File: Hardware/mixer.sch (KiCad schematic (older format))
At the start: 14 parts, among them U5 TL072

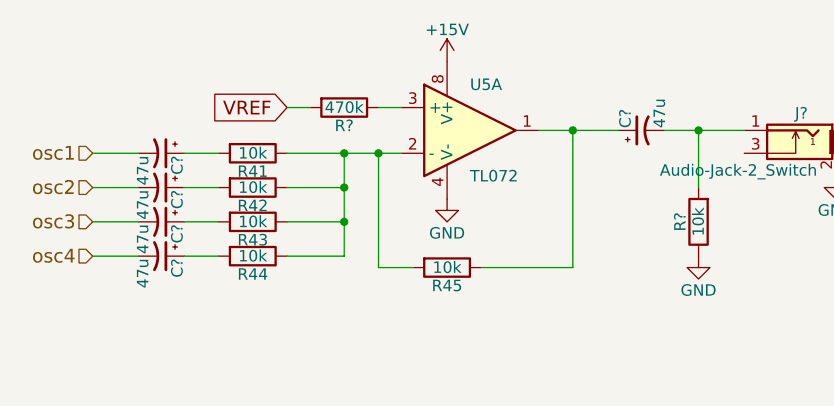
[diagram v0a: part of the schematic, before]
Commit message: change corner frequency of DC blocking caps  everywhere they are in use.  Updated some simulation files to test filter circuits.
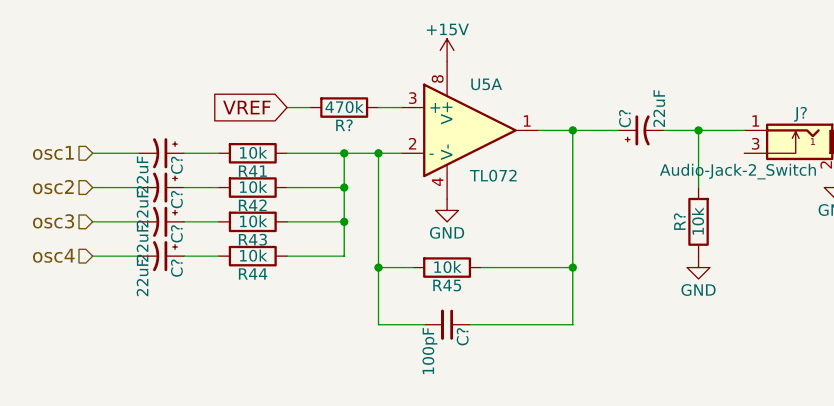
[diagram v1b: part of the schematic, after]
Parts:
- added C?: 100pF, symbol C_Small
- C? (x5): value 47u -> 22uF
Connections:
- net at R41.1, R42.1, R43.1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: now also C?.2
- net at C?.1, R45.1, U5.1: now also C?.1
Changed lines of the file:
@@
 	6200 4100 6600 4100
 Wire Wire Line
-	6600 4100 6600 3500
+	6600 3500 6600 4350
 Wire Wire Line
 	5900 4100 5750 4100
 Wire Wire Line
-	5750 3600 5750 4100
+	5750 3600 5750 4350
 Wire Wire Line
 	5350 3600 5850 3600
@@
 P 4800 3600
 F 0 "C?" H 4810 3670 50  0000 L CNN
-F 1 "47u" H 4810 3520 50  0000 L CNN
+F 1 "22uF" H 4810 3520 50  0000 L CNN
 F 2 "" H 4800 3600 50  0001 C CNN
 F 3 "" H 4800 3600 50  0001 C CNN
@@
 P 4800 3750
 F 0 "C?" H 4810 3820 50  0000 L CNN
-F 1 "47u" H 4810 3670 50  0000 L CNN
+F 1 "22uF" H 4810 3670 50  0000 L CNN
 F 2 "" H 4800 3750 50  0001 C CNN
 F 3 "" H 4800 3750 50  0001 C CNN
@@
 P 4800 3900
 F 0 "C?" H 4810 3970 50  0000 L CNN
-F 1 "47u" H 4810 3820 50  0000 L CNN
+F 1 "22uF" H 4810 3820 50  0000 L CNN
 F 2 "" H 4800 3900 50  0001 C CNN
 F 3 "" H 4800 3900 50  0001 C CNN
@@
 P 4800 4050
 F 0 "C?" H 4810 4120 50  0000 L CNN
-F 1 "47u" H 4810 3970 50  0000 L CNN
+F 1 "22uF" H 4810 3970 50  0000 L CNN
 F 2 "" H 4800 4050 50  0001 C CNN
 F 3 "" H 4800 4050 50  0001 C CNN
@@
 P 6900 3500
 F 0 "C?" H 6910 3570 50  0000 L CNN
-F 1 "47u" H 6910 3420 50  0000 L CNN
+F 1 "22uF" H 6910 3420 50  0000 L CNN
 F 2 "" H 6900 3500 50  0001 C CNN
 F 3 "" H 6900 3500 50  0001 C CNN
@@
 Wire Wire Line
 	5350 3400 5450 3400
+$Comp
+L C_Small C?
+U 1 1 5C37DB67
+P 6050 4350
+F 0 "C?" H 6060 4420 50  0000 L CNN
+F 1 "100pF" H 6060 4270 50  0000 L CNN
+F 2 "" H 6050 4350 50  0001 C CNN
+F 3 "" H 6050 4350 50  0001 C CNN
+	1    6050 4350
+	0    1    1    0
+$EndComp
+Wire Wire Line
+	6600 4350 6150 4350
+Connection ~ 6600 4100
+Wire Wire Line
+	5750 4350 5950 4350
+Connection ~ 5750 4100
 $EndSCHEMATC

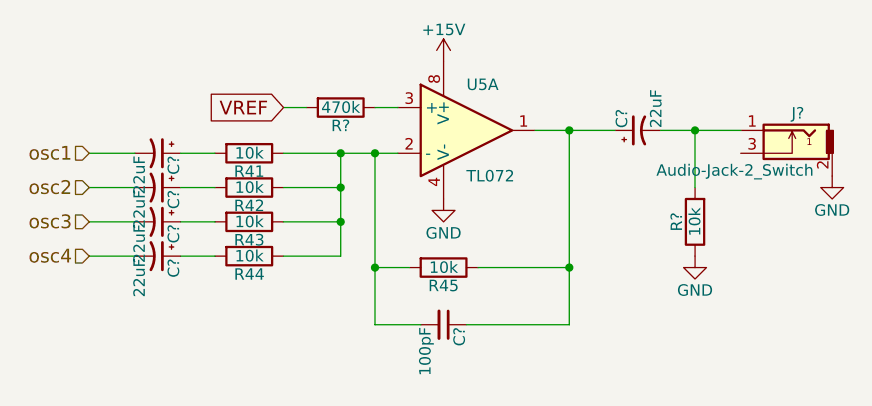
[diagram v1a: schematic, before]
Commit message: associate footprints with all components
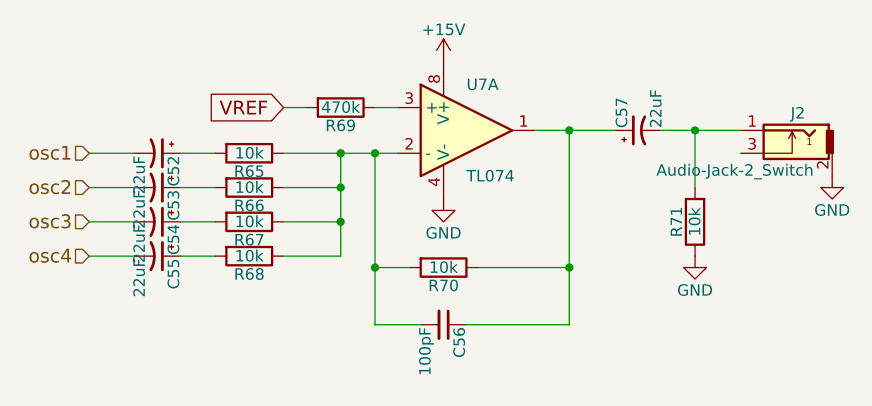
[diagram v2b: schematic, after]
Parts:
- C52, C53, C54, C55, C57: renamed from C?; footprint (none) -> Capacitors_SMD:CP_Elec_5x5.7
- C56: renamed from C?; footprint (none) -> digikey-footprints:0805
- J2: renamed from J?; footprint (none) -> Connectors:PINHEAD1-3
- R65: renamed from R41; footprint (none) -> digikey-footprints:0805
- R66: renamed from R42; footprint (none) -> digikey-footprints:0805
- R67: renamed from R43; footprint (none) -> digikey-footprints:0805
- R68: renamed from R44; footprint (none) -> digikey-footprints:0805
- R69, R71: renamed from R?; footprint (none) -> digikey-footprints:0805
- R70: renamed from R45; footprint (none) -> digikey-footprints:0805
- U7: renamed from U5; value TL072 -> TL074; footprint (none) -> digikey-footprints:Humidity_SHT15
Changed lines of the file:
@@
 osc4
 $Comp
-L R R41
+L R R65
 U 1 1 5C368A69
 P 5200 3600
-F 0 "R41" V 5280 3600 50  0000 C CNN
+F 0 "R65" V 5280 3600 50  0000 C CNN
 F 1 "10k" V 5200 3600 50  0000 C CNN
-F 2 "" V 5130 3600 50  0001 C CNN
+F 2 "digikey-footprints:0805" V 5130 3600 50  0001 C CNN
 F 3 "" H 5200 3600 50  0001 C CNN
 	1    5200 3600
@@
 $EndComp
 $Comp
-L R R42
+L R R66
 U 1 1 5C368B13
 P 5200 3750
-F 0 "R42" V 5280 3750 50  0000 C CNN
+F 0 "R66" V 5280 3750 50  0000 C CNN
 F 1 "10k" V 5200 3750 50  0000 C CNN
-F 2 "" V 5130 3750 50  0001 C CNN
+F 2 "digikey-footprints:0805" V 5130 3750 50  0001 C CNN
 F 3 "" H 5200 3750 50  0001 C CNN
 	1    5200 3750
@@
 $EndComp
 $Comp
-L R R43
+L R R67
 U 1 1 5C368B2B
 P 5200 3900
-F 0 "R43" V 5280 3900 50  0000 C CNN
+F 0 "R67" V 5280 3900 50  0000 C CNN
 F 1 "10k" V 5200 3900 50  0000 C CNN
-F 2 "" V 5130 3900 50  0001 C CNN
+F 2 "digikey-footprints:0805" V 5130 3900 50  0001 C CNN
 F 3 "" H 5200 3900 50  0001 C CNN
 	1    5200 3900
@@
 $EndComp
 $Comp
-L R R44
+L R R68
 U 1 1 5C368B46
 P 5200 4050
-F 0 "R44" V 5280 4050 50  0000 C CNN
+F 0 "R68" V 5280 4050 50  0000 C CNN
 F 1 "10k" V 5200 4050 50  0000 C CNN
-F 2 "" V 5130 4050 50  0001 C CNN
+F 2 "digikey-footprints:0805" V 5130 4050 50  0001 C CNN
 F 3 "" H 5200 4050 50  0001 C CNN
 	1    5200 4050
@@
 	4500 4050 4700 4050
 $Comp
-L TL072 U5
+L TL072 U7
 U 1 1 5C368C88
 P 6150 3500
-F 0 "U5" H 6150 3700 50  0000 L CNN
-F 1 "TL072" H 6150 3300 50  0000 L CNN
-F 2 "" H 6150 3500 50  0001 C CNN
+F 0 "U7" H 6150 3700 50  0000 L CNN
+F 1 "TL074" H 6150 3300 50  0000 L CNN
+F 2 "digikey-footprints:Humidity_SHT15" H 6150 3500 50  0001 C CNN
 F 3 "" H 6150 3500 50  0001 C CNN
 	1    6150 3500
@@
 $EndComp
 $Comp
-L R R45
+L R R70
 U 1 1 5C368D28
 P 6050 4100
-F 0 "R45" V 6130 4100 50  0000 C CNN
+F 0 "R70" V 6130 4100 50  0000 C CNN
 F 1 "10k" V 6050 4100 50  0000 C CNN
-F 2 "" V 5980 4100 50  0001 C CNN
+F 2 "digikey-footprints:0805" V 5980 4100 50  0001 C CNN
 F 3 "" H 6050 4100 50  0001 C CNN
 	1    6050 4100
@@
 Connection ~ 6600 3500
 $Comp
-L Audio-Jack-2_Switch J?
+L Audio-Jack-2_Switch J2
 U 1 1 5C394BFE
 P 7550 3600
-F 0 "J?" H 7500 3775 50  0000 C CNN
+F 0 "J2" H 7500 3775 50  0000 C CNN
 F 1 "Audio-Jack-2_Switch" H 7775 3525 50  0000 C CNN
-F 2 "" H 7800 3700 50  0001 C CNN
+F 2 "Connectors:PINHEAD1-3" H 7800 3700 50  0001 C CNN
 F 3 "" H 7800 3700 50  0001 C CNN
 	1    7550 3600
@@
 $EndComp
 $Comp
-L GND #PWR?
+L GND #PWR067
 U 1 1 5C394C8E
 P 7750 3700
-F 0 "#PWR?" H 7750 3450 50  0001 C CNN
+F 0 "#PWR067" H 7750 3450 50  0001 C CNN
 F 1 "GND" H 7750 3550 50  0000 C CNN
 F 2 "" H 7750 3700 50  0001 C CNN
@@
 $EndComp
 $Comp
-L CP1_Small C?
+L CP1_Small C52
 U 1 1 5C396119
 P 4800 3600
-F 0 "C?" H 4810 3670 50  0000 L CNN
+F 0 "C52" H 4810 3670 50  0000 L CNN
 F 1 "22uF" H 4810 3520 50  0000 L CNN
-F 2 "" H 4800 3600 50  0001 C CNN
+F 2 "Capacitors_SMD:CP_Elec_5x5.7" H 4800 3600 50  0001 C CNN
 F 3 "" H 4800 3600 50  0001 C CNN
 	1    4800 3600
@@
 $EndComp
 $Comp
-L CP1_Small C?
+L CP1_Small C53
 U 1 1 5C396261
 P 4800 3750
-F 0 "C?" H 4810 3820 50  0000 L CNN
+F 0 "C53" H 4810 3820 50  0000 L CNN
 F 1 "22uF" H 4810 3670 50  0000 L CNN
-F 2 "" H 4800 3750 50  0001 C CNN
+F 2 "Capacitors_SMD:CP_Elec_5x5.7" H 4800 3750 50  0001 C CNN
 F 3 "" H 4800 3750 50  0001 C CNN
 	1    4800 3750
@@
 $EndComp
 $Comp
-L CP1_Small C?
+L CP1_Small C54
 U 1 1 5C39628E
 P 4800 3900
-F 0 "C?" H 4810 3970 50  0000 L CNN
+F 0 "C54" H 4810 3970 50  0000 L CNN
 F 1 "22uF" H 4810 3820 50  0000 L CNN
-F 2 "" H 4800 3900 50  0001 C CNN
+F 2 "Capacitors_SMD:CP_Elec_5x5.7" H 4800 3900 50  0001 C CNN
 F 3 "" H 4800 3900 50  0001 C CNN
 	1    4800 3900
@@
 $EndComp
 $Comp
-L CP1_Small C?
+L CP1_Small C55
 U 1 1 5C3962BE
 P 4800 4050
-F 0 "C?" H 4810 4120 50  0000 L CNN
+F 0 "C55" H 4810 4120 50  0000 L CNN
 F 1 "22uF" H 4810 3970 50  0000 L CNN
-F 2 "" H 4800 4050 50  0001 C CNN
+F 2 "Capacitors_SMD:CP_Elec_5x5.7" H 4800 4050 50  0001 C CNN
 F 3 "" H 4800 4050 50  0001 C CNN
 	1    4800 4050
@@
 	4900 3600 5050 3600
 $Comp
-L GND #PWR?
+L GND #PWR068
 U 1 1 5C396479
 P 6050 3800
-F 0 "#PWR?" H 6050 3550 50  0001 C CNN
+F 0 "#PWR068" H 6050 3550 50  0001 C CNN
 F 1 "GND" H 6050 3650 50  0000 C CNN
 F 2 "" H 6050 3800 50  0001 C CNN
@@
 $EndComp
 $Comp
-L CP1_Small C?
+L CP1_Small C57
 U 1 1 5C3964A5
 P 6900 3500
-F 0 "C?" H 6910 3570 50  0000 L CNN
+F 0 "C57" H 6910 3570 50  0000 L CNN
 F 1 "22uF" H 6910 3420 50  0000 L CNN
-F 2 "" H 6900 3500 50  0001 C CNN
+F 2 "Capacitors_SMD:CP_Elec_5x5.7" H 6900 3500 50  0001 C CNN
 F 3 "" H 6900 3500 50  0001 C CNN
 	1    6900 3500
@@
 	7000 3500 7350 3500
 $Comp
-L R R?
+L R R71
 U 1 1 5C3965C9
 P 7150 3900
-F 0 "R?" V 7230 3900 50  0000 C CNN
+F 0 "R71" V 7230 3900 50  0000 C CNN
 F 1 "10k" V 7150 3900 50  0000 C CNN
-F 2 "" V 7080 3900 50  0001 C CNN
+F 2 "digikey-footprints:0805" V 7080 3900 50  0001 C CNN
 F 3 "" H 7150 3900 50  0001 C CNN
 	1    7150 3900
@@
 Connection ~ 7150 3500
 $Comp
-L GND #PWR?
+L GND #PWR069
 U 1 1 5C39665C
 P 7150 4050
-F 0 "#PWR?" H 7150 3800 50  0001 C CNN
+F 0 "#PWR069" H 7150 3800 50  0001 C CNN
 F 1 "GND" H 7150 3900 50  0000 C CNN
 F 2 "" H 7150 4050 50  0001 C CNN
@@
 $EndComp
 $Comp
-L +15V #PWR?
+L +15V #PWR070
 U 1 1 5C396690
 P 6050 3200
-F 0 "#PWR?" H 6050 3050 50  0001 C CNN
+F 0 "#PWR070" H 6050 3050 50  0001 C CNN
 F 1 "+15V" H 6050 3340 50  0000 C CNN
 F 2 "" H 6050 3200 50  0001 C CNN
@@
 VREF
 $Comp
-L R R?
+L R R69
 U 1 1 5C39670B
 P 5600 3400
-F 0 "R?" V 5680 3400 50  0000 C CNN
+F 0 "R69" V 5680 3400 50  0000 C CNN
 F 1 "470k" V 5600 3400 50  0000 C CNN
-F 2 "" V 5530 3400 50  0001 C CNN
+F 2 "digikey-footprints:0805" V 5530 3400 50  0001 C CNN
 F 3 "" H 5600 3400 50  0001 C CNN
 	1    5600 3400
@@
 	5350 3400 5450 3400
 $Comp
-L C_Small C?
+L C_Small C56
 U 1 1 5C37DB67
 P 6050 4350
-F 0 "C?" H 6060 4420 50  0000 L CNN
+F 0 "C56" H 6060 4420 50  0000 L CNN
 F 1 "100pF" H 6060 4270 50  0000 L CNN
-F 2 "" H 6050 4350 50  0001 C CNN
+F 2 "digikey-footprints:0805" H 6050 4350 50  0001 C CNN
 F 3 "" H 6050 4350 50  0001 C CNN
 	1    6050 4350

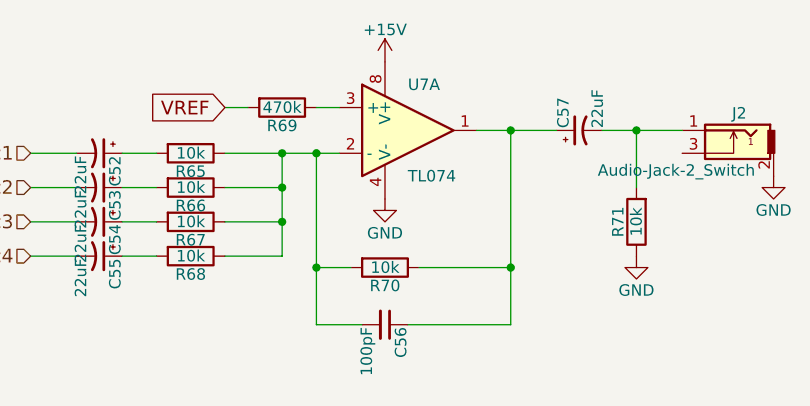
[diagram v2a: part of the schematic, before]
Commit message: fix annotation and footprints for multi-part op amps.
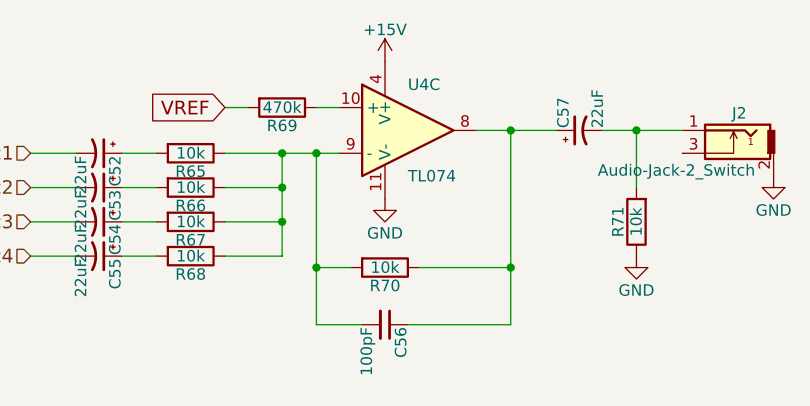
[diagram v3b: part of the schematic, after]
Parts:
- removed U7: TL074, digikey-footprints:Humidity_SHT15, symbol TL072
- added U4: TL074, digikey-footprints:SOIC-14_W3.9mm, symbol TL074
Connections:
- net +15V: now also U4.4 (V+)
- net GND: now also U4.11 (V-)
- net at C56.2, R65.1, R66.1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: now also U4.9 (-)
- net at C56.1, C57.1, R70.1: now also U4.8
- net at R69.1: now also U4.10 (+)
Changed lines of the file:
@@
 	4500 4050 4700 4050
-$Comp
-L TL072 U7
-U 1 1 5C368C88
-P 6150 3500
-F 0 "U7" H 6150 3700 50  0000 L CNN
-F 1 "TL074" H 6150 3300 50  0000 L CNN
-F 2 "digikey-footprints:Humidity_SHT15" H 6150 3500 50  0001 C CNN
-F 3 "" H 6150 3500 50  0001 C CNN
-	1    6150 3500
-	1    0    0    -1
-$EndComp
 $Comp
 L R R70
@@
 	5750 4350 5950 4350
 Connection ~ 5750 4100
+$Comp
+L TL074 U4
+U 3 1 5C3DF7DA
+P 6150 3500
+F 0 "U4" H 6150 3700 50  0000 L CNN
+F 1 "TL074" H 6150 3300 50  0000 L CNN
+F 2 "digikey-footprints:SOIC-14_W3.9mm" H 6100 3600 50  0001 C CNN
+F 3 "" H 6200 3700 50  0001 C CNN
+	3    6150 3500
+	1    0    0    -1
+$EndComp
 $EndSCHEMATC

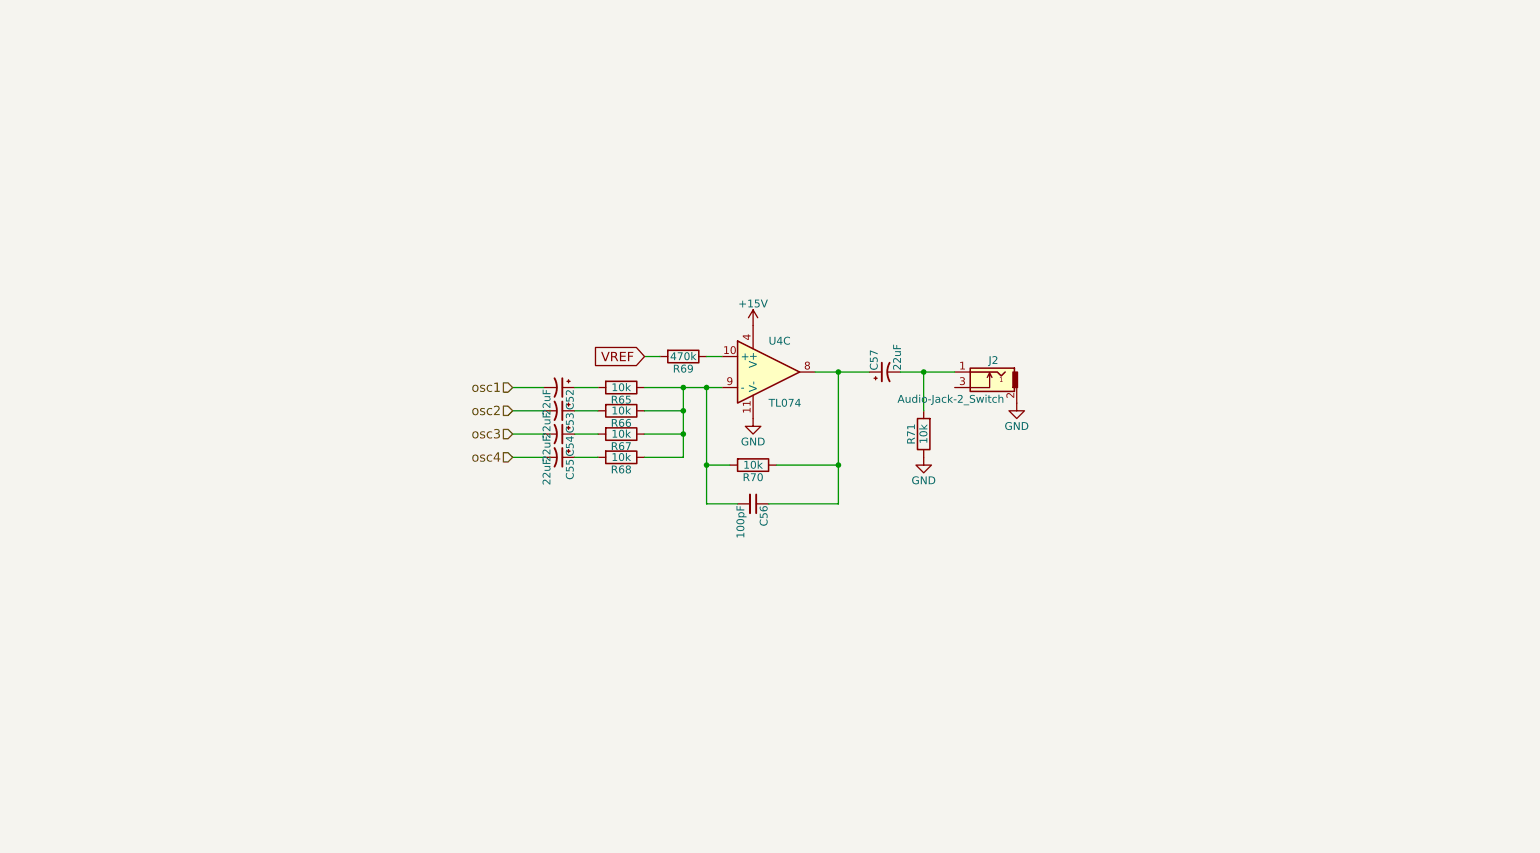
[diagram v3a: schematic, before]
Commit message: simulate bias voltage buffer. Previous op amp approach couldn't go close enough to the rails.
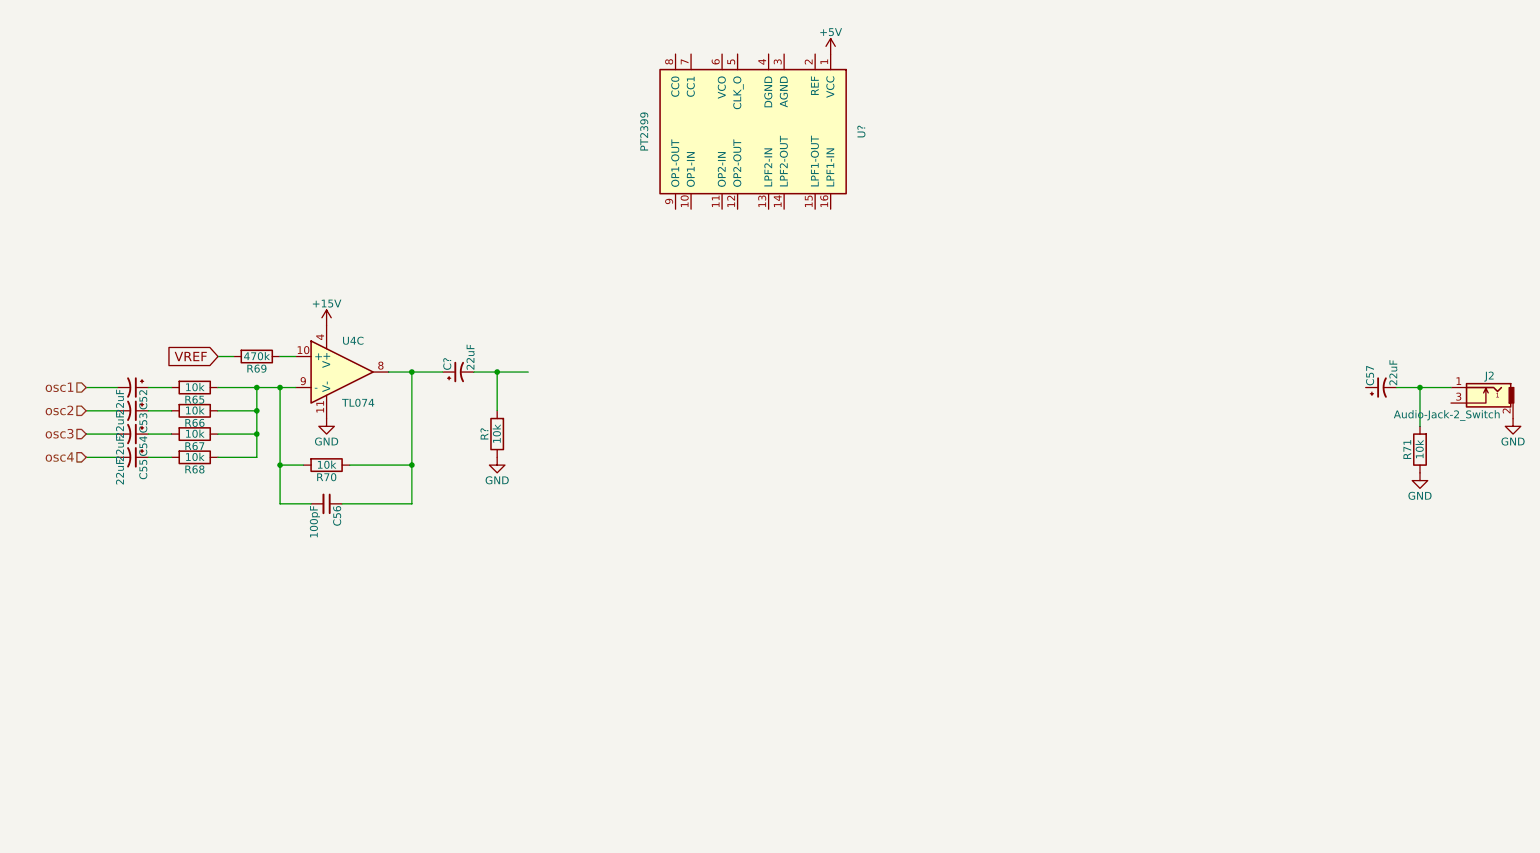
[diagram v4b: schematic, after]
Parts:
- added C?: 22uF, Capacitors_SMD:CP_Elec_5x5.7, symbol CP1_Small
- added R?: 10k, digikey-footprints:0805, symbol R
- added U?: PT2399, symbol PT2399
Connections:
- net labels added: +5V
- wire segments 24 -> 26
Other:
- moved on the sheet: C52, C53, C54, C55, C56, C57, J2, R65, R66, R67, R68, R69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
